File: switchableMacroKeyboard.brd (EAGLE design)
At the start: 58.4 x 110.5 mm, 36 parts

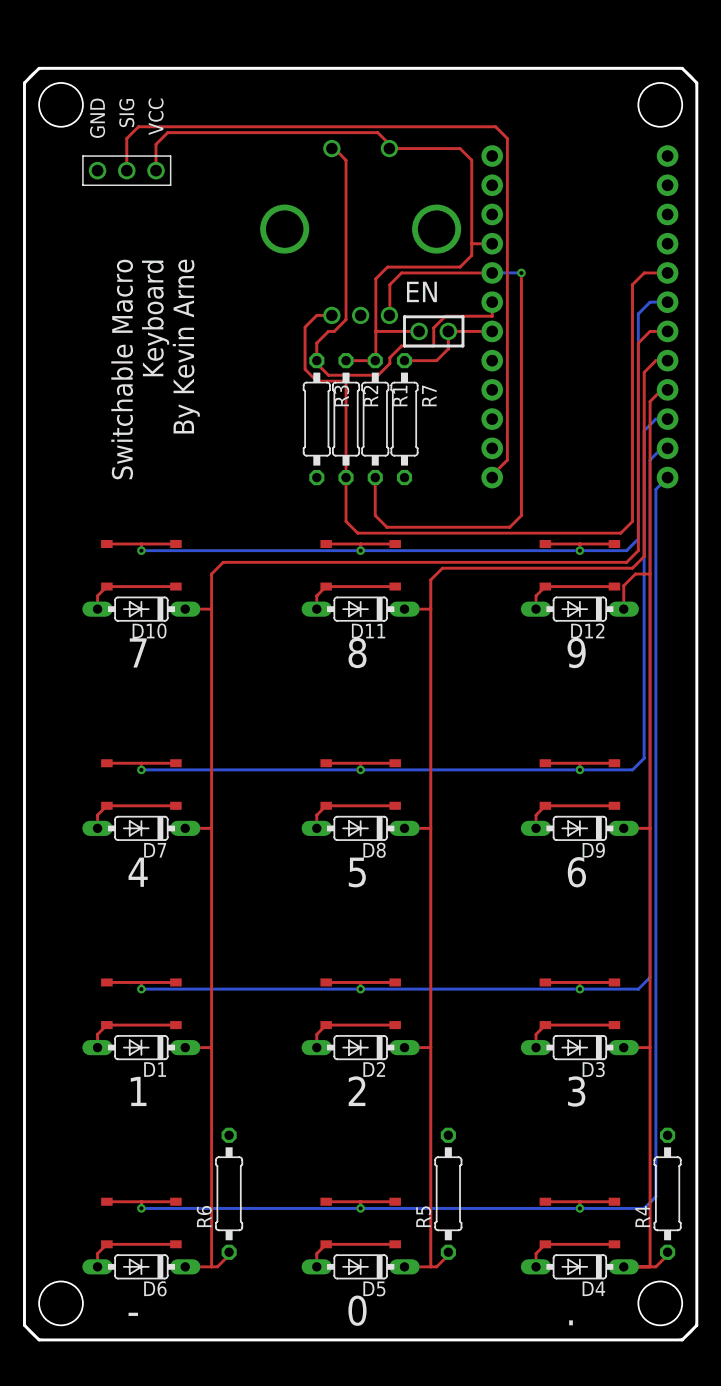
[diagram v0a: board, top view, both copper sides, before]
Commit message: Added I2C header for LCD panel. Rearranged pinouts to open up I2C pins on the Pro Micro. To do: add labels to I2C bus and reroute board.
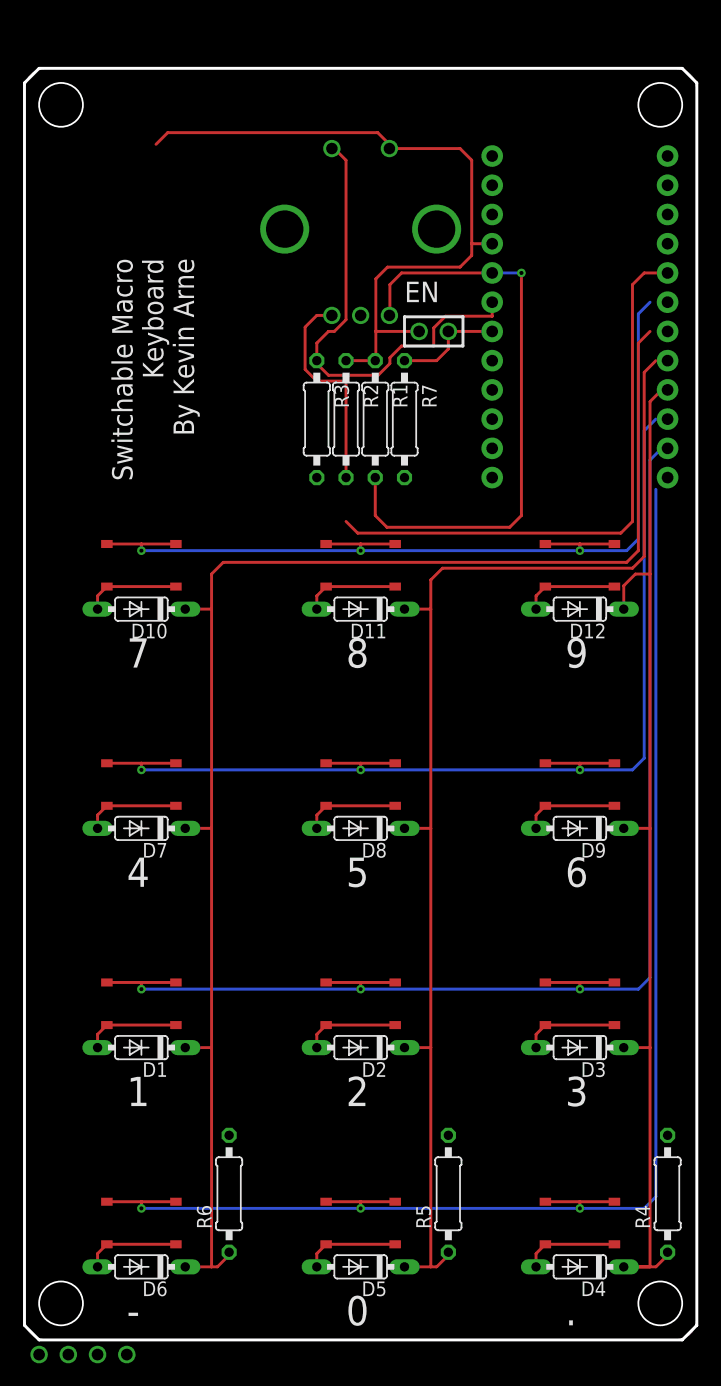
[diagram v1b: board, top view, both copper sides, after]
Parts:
- removed U$14: 100MIL3PINSIGNAL, switchableMacroKeyboard:100MIL3PINSIGNAL
- added U$3: I2C-100MIL, ARNEConnectors:I2C-100MIL
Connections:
- net N$10 renamed ROW2
- net N$2 renamed ROW3
- net N$22 renamed COL1
- net N$28 renamed COL0
- net N$30 renamed COL2
- removed net LCDSIG: B1.13, U$14.SIG
- removed net N$12: B1.5, R2.2, U$13.A
- removed net N$17: 10.1, 10.2, 11.1, 11.2, 12.1, 12.2, B1.10
- removed net N$24: 00.1, 00.2, 01.1, 01.2, 02.1, 02.2, B1.6
- new net N$1: B1.10, R2.2, U$13.A
- new net ROW0: 00.1, 00.2, 01.1, 01.2, 02.1, 02.2, B1.17
- new net ROW1: 10.1, 10.2, 11.1, 11.2, 12.1, 12.2, B1.13
- new net SCL: B1.6, U$3.SCL
- new net SDA: B1.5, U$3.SDA
- net GND: now also U$3.GND; no longer U$14.GND
- net VCC: now also U$3.VCC; no longer U$14.VCC
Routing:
- net N$17: track 94.7 -> 0.00 mm, vias 3 -> 0
- net ROW1: track 0.00 -> 93.7 mm, vias 0 -> 3
- net N$24: track 85.9 -> 0.00 mm, vias 3 -> 0
- net ROW0: track 0.00 -> 84.3 mm, vias 0 -> 3
- net N$12: track 72.4 -> 0.00 mm
- net LCDSIG: track 66.7 -> 0.00 mm
- net SDA: track 0.00 -> 49.8 mm
- net N$1: track 0.00 -> 18.8 mm
- net VCC: track 64.0 -> 61.7 mm
- net COL0: track 130.5 -> 128.9 mm
- net ROW3: track 127.8 -> 126.3 mm
- net COL1: track 108.9 -> 107.9 mm
- net ROW2: track 111.3 -> 110.8 mm
- net COL2: track 93.2 -> 92.7 mm

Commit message: Partially rerouted board with several pins moved around on the microcontroller for ease of routing. To do: route columns on bottom layer.
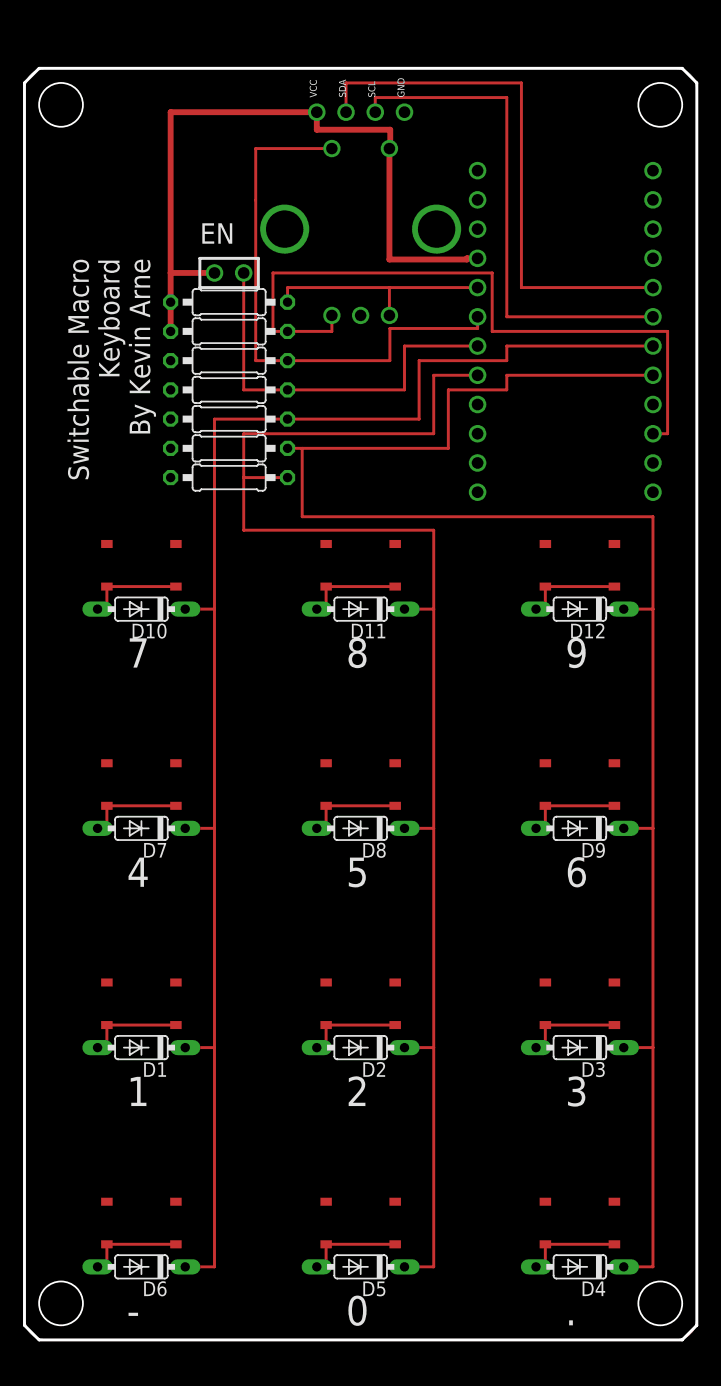
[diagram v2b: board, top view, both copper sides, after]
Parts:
- moved U$3 110.6 mm to (29.2, 106.7)
- moved R4 75.1 mm to (17.8, 77.5), turned to 180 degrees
- moved R6 67.3 mm to (17.8, 80.0), turned to 180 degrees
- moved R5 65.1 mm to (17.8, 74.9), turned to 180 degrees
- moved U$1 18.5 mm to (16.5, 92.7)
- moved U$2 18.5 mm to (19.1, 92.7)
- moved R1 16.3 mm to (17.8, 90.2), turned to 0 degrees
- moved R7 15.5 mm to (17.8, 82.5), turned to 180 degrees
- moved R2 12.7 mm to (17.8, 87.6), turned to 0 degrees
- moved R3 9.16 mm to (17.8, 85.1), turned to 180 degrees
- moved B1 1.80 mm to (47.0, 88.9)
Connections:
- net COL1: now also B1.17; no longer B1.8
- net COL2: now also B1.8; no longer B1.9
- net ROW0: now also B1.9; no longer B1.17
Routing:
- net ROW3: track 126.3 -> 0.00 mm, vias 3 -> 0
- net ROW2: track 110.8 -> 0.00 mm, vias 3 -> 0
- net ROW1: track 93.7 -> 0.00 mm, vias 3 -> 0
- net ROW0: track 84.3 -> 0.00 mm, vias 3 -> 0
- net COL2: track 92.7 -> 149.9 mm
- net SCL: track 0.00 -> 44.4 mm
- net N$1: track 18.8 -> 61.1 mm
- net N$9: track 52.5 -> 20.2 mm, vias 1 -> 0
- net EN: track 9.56 -> 34.3 mm
- net COL1: track 107.9 -> 128.3 mm
- net SW-SIG: track 40.9 -> 48.1 mm
- net SDA: track 49.8 -> 47.0 mm
- net VCC: track 61.7 -> 62.5 mm
- net COL0: track 128.9 -> 128.3 mm

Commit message: Added a header file to hold all of the keyboards. Added an LCD test that works.
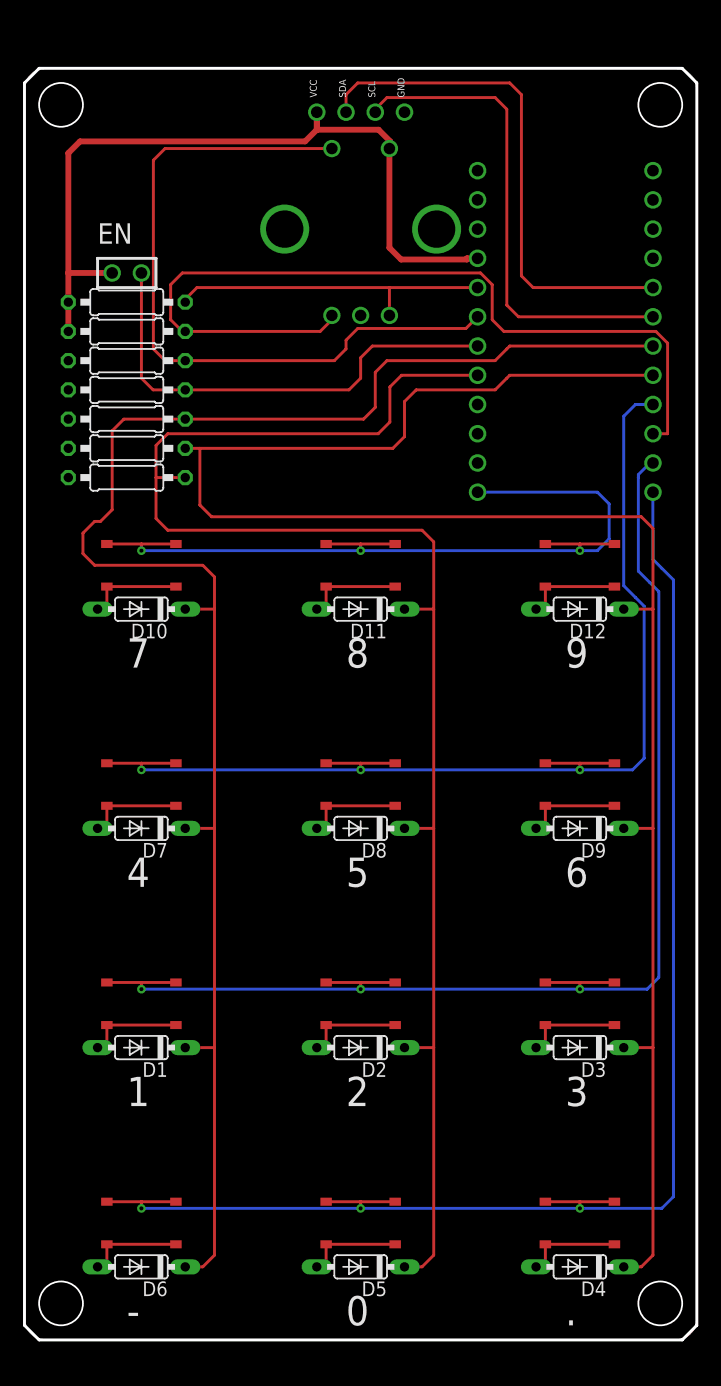
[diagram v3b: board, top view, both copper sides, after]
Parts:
- moved R1 8.89 mm to (8.89, 90.2)
- moved R2 8.89 mm to (8.89, 87.6)
- moved R3 8.89 mm to (8.89, 85.1)
- moved R4 8.89 mm to (8.89, 77.5)
- moved R5 8.89 mm to (8.89, 74.9)
- moved R6 8.89 mm to (8.89, 80.0)
- moved R7 8.89 mm to (8.89, 82.5)
- moved U$1 8.89 mm to (7.62, 92.7)
- moved U$2 8.89 mm to (10.2, 92.7)
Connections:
- net ROW0: now also B1.13; no longer B1.9
- net ROW1: now also B1.9; no longer B1.13
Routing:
- net ROW3: track 0.00 -> 128.3 mm, vias 0 -> 3
- net ROW2: track 0.00 -> 111.2 mm, vias 0 -> 3
- net ROW1: track 0.00 -> 97.3 mm, vias 0 -> 3
- net ROW0: track 0.00 -> 75.7 mm, vias 0 -> 3
- net COL0: track 128.3 -> 145.6 mm
- net SW-SIG: track 48.1 -> 62.9 mm
- net N$1: track 61.1 -> 75.3 mm
- net COL2: track 149.9 -> 163.9 mm
- net COL1: track 128.3 -> 138.7 mm
- net N$9: track 20.2 -> 28.5 mm
- net EN: track 34.3 -> 41.4 mm
- net VCC: track 62.5 -> 69.0 mm
- net SDA: track 47.0 -> 45.2 mm
- net SCL: track 44.4 -> 42.7 mm

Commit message: Switched the buttons to Cherry MX Blues, but found this may require a bigger board, mostly length-wise. Moving the diodes out of the way of the key has cramped things. To do: adjust board dimensions to fit new buttons, reroute keypad traces.
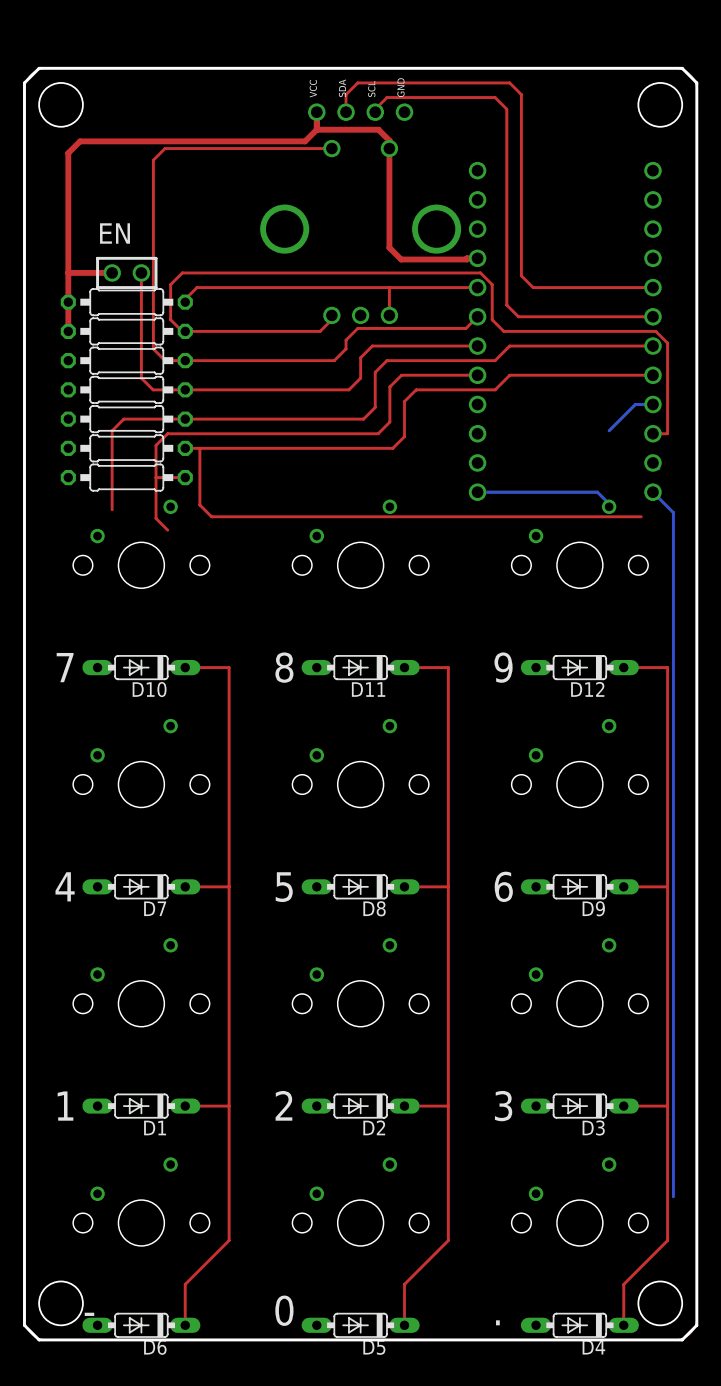
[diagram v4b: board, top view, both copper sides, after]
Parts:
- removed 00, 01, 02, 10, 11, 12, 20, 21, 22, 30, 31, 32: TACT-PTS526-SMG15-SMTR2-LFS, ARNEInput:TACT-PTS526-SMTR2-LFS
- added U$10, U$11, U$12, U$14, U$15, U$16, U$4, U$5, U$6, U$7, U$8, U$9: CHERRYMXBLUE, ARNEInput:CHERRYMXBLUE
- moved D7 5.08 mm to (10.2, 39.4)
- moved D8 5.08 mm to (29.2, 39.4)
- moved D9 5.08 mm to (48.3, 39.4)
- moved D4 5.08 mm to (48.3, 1.27)
- moved D5 5.08 mm to (29.2, 1.27)
- moved D6 5.08 mm to (10.2, 1.27)
- moved D1 5.08 mm to (10.2, 20.3)
- moved D10 5.08 mm to (10.2, 58.4)
- moved D11 5.08 mm to (29.2, 58.4)
- moved D12 5.08 mm to (48.3, 58.4)
- moved D2 5.08 mm to (29.2, 20.3)
- moved D3 5.08 mm to (48.3, 20.3)
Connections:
- net N$18: now also U$7.P$1; no longer 10.3, 10.4
- net N$19: now also U$8.P$1; no longer 11.3, 11.4
- net N$20: now also U$9.P$1; no longer 12.3, 12.4
- net N$25: now also U$4.P$1; no longer 00.3, 00.4
- net N$26: now also U$5.P$1; no longer 01.3, 01.4
- net N$27: now also U$6.P$1; no longer 02.3, 02.4
- net N$3: now also U$10.P$1; no longer 20.3, 20.4
- net N$4: now also U$11.P$1; no longer 21.3, 21.4
- net N$5: now also U$12.P$1; no longer 22.3, 22.4
- net N$6: now also U$14.P$1; no longer 30.3, 30.4
- net N$7: now also U$15.P$1; no longer 31.3, 31.4
- net N$8: now also U$16.P$1; no longer 32.3, 32.4
- net ROW0: now also U$4.P$2, U$5.P$2, U$6.P$2; no longer 00.1, 00.2, 01.1, 01.2, 02.1, 02.2
- net ROW1: now also U$7.P$2, U$8.P$2, U$9.P$2; no longer 10.1, 10.2, 11.1, 11.2, 12.1, 12.2
- net ROW2: now also U$10.P$2, U$11.P$2, U$12.P$2; no longer 20.1, 20.2, 21.1, 21.2, 22.1, 22.2
- net ROW3: now also U$14.P$2, U$15.P$2, U$16.P$2; no longer 30.1, 30.2, 31.1, 31.2, 32.1, 32.2
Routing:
- net ROW2: track 111.2 -> 0.72 mm, vias 3 -> 0
- net ROW1: track 97.3 -> 4.76 mm, vias 3 -> 0
- net ROW3: track 128.3 -> 62.0 mm, vias 3 -> 0
- net ROW0: track 75.7 -> 11.9 mm, vias 3 -> 0
- net COL1: track 138.7 -> 112.7 mm
- net COL0: track 145.6 -> 128.8 mm
- net N$8: track 8.77 -> 0.81 mm
- net N$7: track 8.77 -> 0.81 mm
- net N$6: track 8.77 -> 0.81 mm
- net N$5: track 8.77 -> 0.81 mm
- net N$4: track 8.77 -> 0.81 mm
- net N$3: track 8.77 -> 0.81 mm
- net N$27: track 8.77 -> 0.81 mm
- net N$26: track 8.77 -> 0.81 mm
- net N$25: track 8.77 -> 0.81 mm
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
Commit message: Adjusted the size of the board and rerouted.
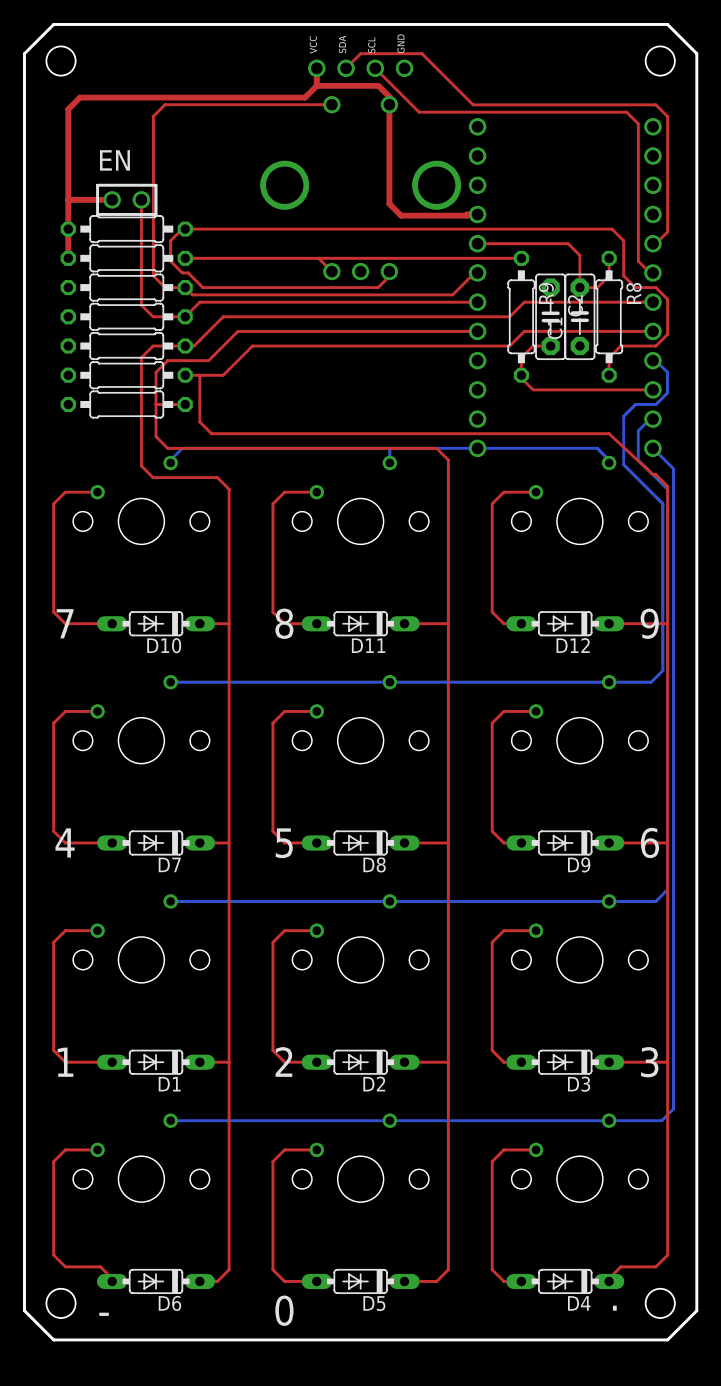
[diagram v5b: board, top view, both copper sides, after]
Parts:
- added C1, C2: (no value), capacitor-wima:C5B2.5
- added R8, R9: 10k, rcl:0207/10
- moved R2 6.35 mm to (8.89, 94.0)
- moved R7 6.35 mm to (8.89, 88.9)
- moved U$1 6.35 mm to (7.62, 99.1)
- moved U$2 6.35 mm to (10.2, 99.1)
- moved R1 6.35 mm to (8.89, 96.5)
- moved R3 6.35 mm to (8.89, 91.4)
- moved R4 6.35 mm to (8.89, 83.8)
- moved R5 6.35 mm to (8.89, 81.3)
- moved R6 6.35 mm to (8.89, 86.4)
- moved D7 4.02 mm to (11.4, 43.2)
- moved D9 4.02 mm to (47.0, 43.2)
- moved D6 4.02 mm to (11.4, 5.08)
- moved D1 4.02 mm to (11.4, 24.1)
- moved D4 4.02 mm to (47.0, 5.08)
- moved D3 4.02 mm to (47.0, 24.1)
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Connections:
- new net N$10: R2.2, R9.1, U$13.A
- new net N$2: R1.2, R8.2, U$13.B
- net GND: now also C1.1, C2.1
- net N$1: now also C2.2, R9.2; no longer R2.2, U$13.A
- net N$9: now also C1.2, R8.1; no longer R1.2, U$13.B
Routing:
- net ROW2: track 0.72 -> 86.2 mm
- net N$2: track 0.00 -> 81.0 mm
- net ROW1: track 4.76 -> 74.8 mm
- net N$1: track 75.3 -> 16.6 mm
- net ROW3: track 62.0 -> 102.2 mm
- net COL1: track 112.7 -> 149.8 mm
- net N$10: track 0.00 -> 30.8 mm
- net ROW0: track 11.9 -> 40.7 mm
- net COL2: track 158.9 -> 177.4 mm
- net N$3: track 0.81 -> 19.1 mm
- net N$25: track 0.81 -> 19.1 mm
- net N$18: track 0.81 -> 19.1 mm
- net N$6: track 0.81 -> 18.5 mm
- net N$4: track 0.81 -> 17.9 mm
- net N$7: track 0.81 -> 17.9 mm
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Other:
- board size 58.4 x 110.5 mm -> 58.4 x 114.3 mm
